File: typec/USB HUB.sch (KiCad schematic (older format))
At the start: 26 parts, among them U1 TPD6E05U06-USON, U2 TPD4E05U06-USON, U3 TPS62081-WSON, U4 TPD4E05U06-USON, U5 TPS74801-VSON, U6 TUSB212-X2QFN

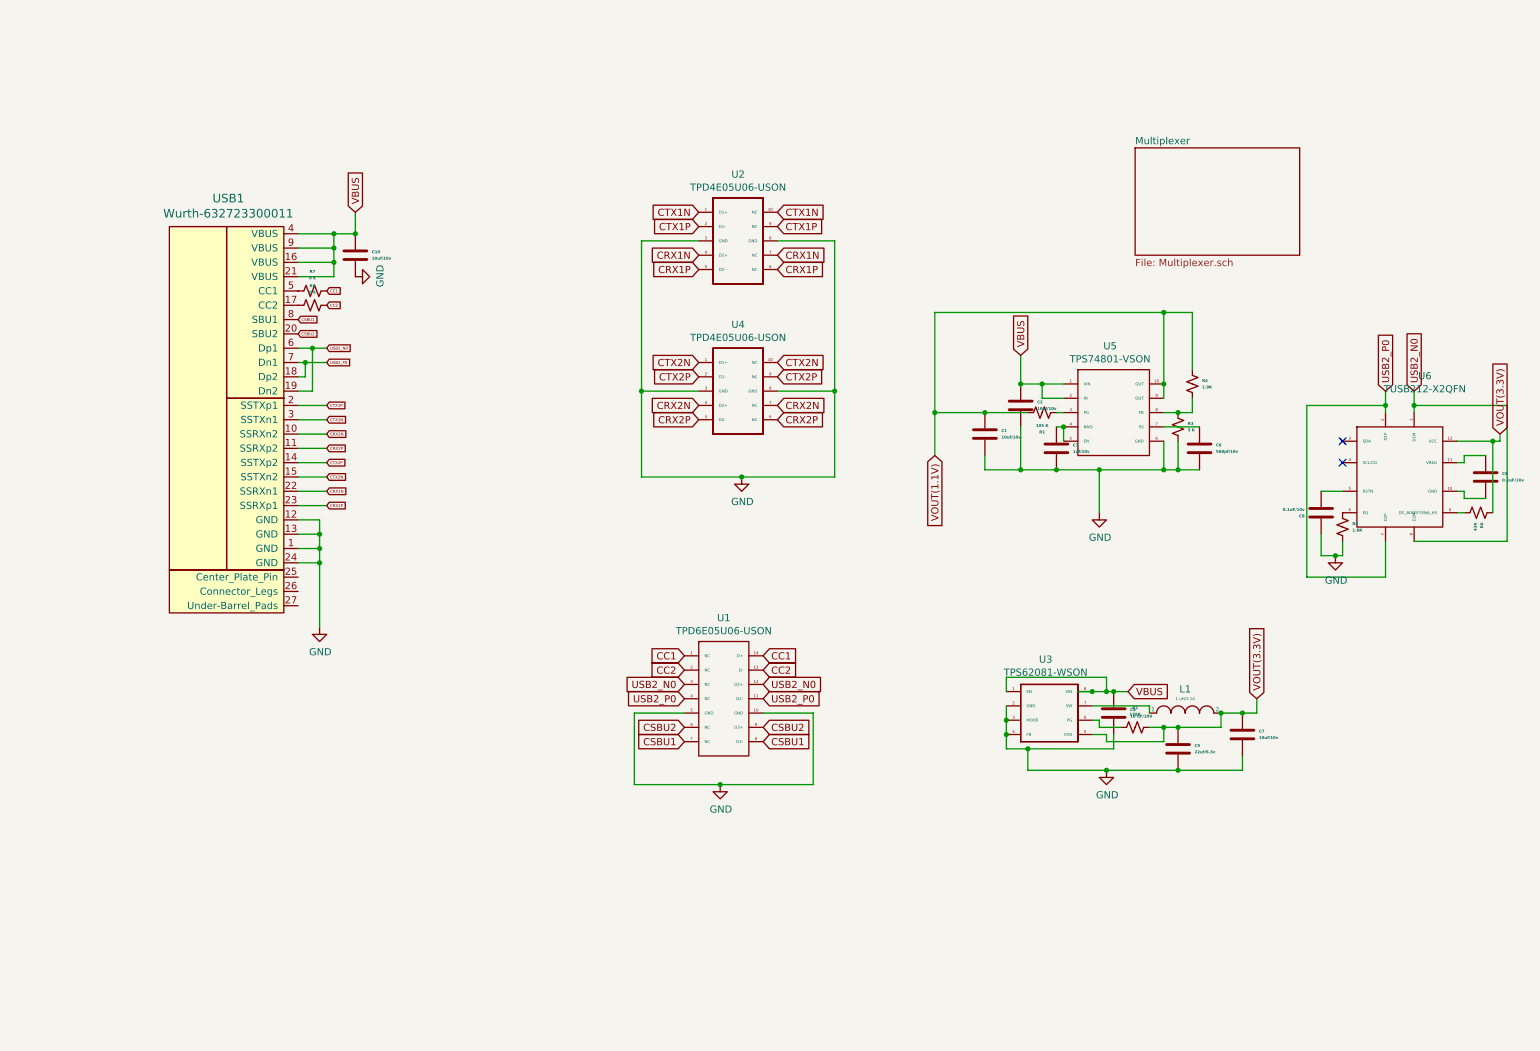
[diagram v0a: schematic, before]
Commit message: Added another page and completed the Multiplexer schematics.
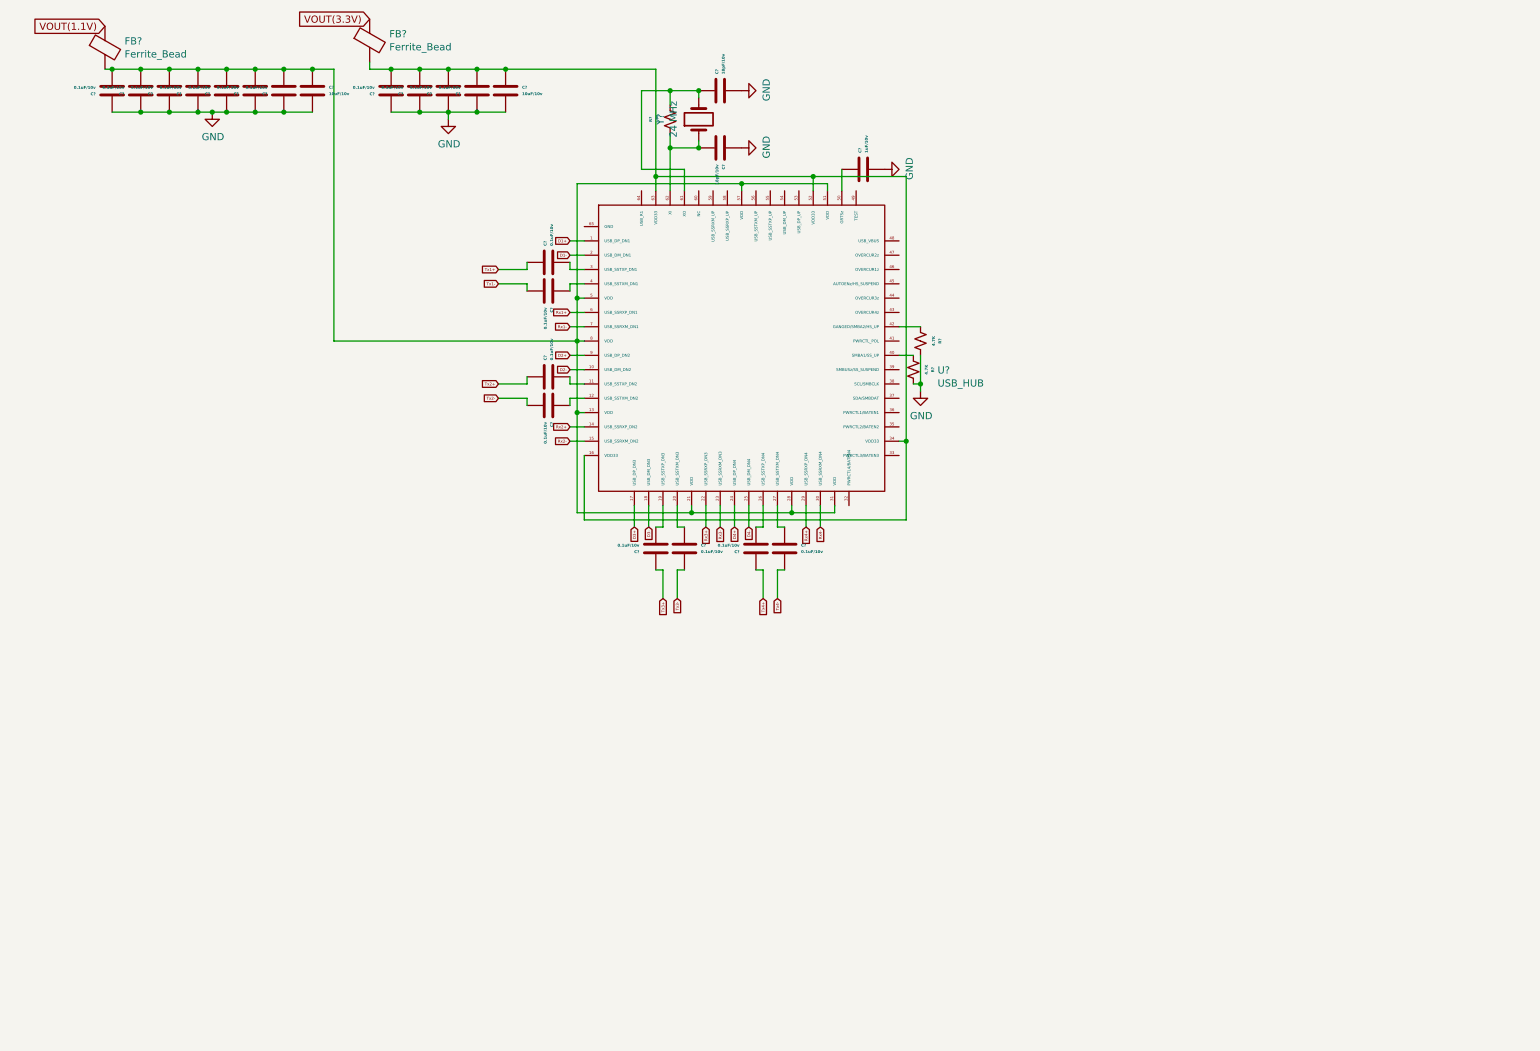
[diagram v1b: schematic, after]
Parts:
- removed C1, C10, C2, C7: 10uf/10v, Capacitor_SMD:C_0805_2012Metric, symbol Device:C
- removed C3: 1uf/10v, Capacitor_SMD:C_0402_1005Metric, symbol Device:C
- removed C4: 10 uF/10V, Capacitor_SMD:C_0805_2012Metric, symbol Device:C
- removed C5: 22uf/6.3v, Capacitor_SMD:C_0805_2012Metric, symbol Device:C
- removed C6: 560pf/10v, Capacitor_SMD:C_0402_1005Metric, symbol Device:C
- removed C8, C9: 0.1uF/10v, Capacitor_SMD:C_0402_1005Metric, symbol Device:C
- removed L1: 1 uH/3.1A, Inductor_SMD:L_6.3x6.3_H3, symbol pspice:INDUCTOR
- removed R1: 105 K, Resistor_SMD:R_0805_2012Metric, symbol Device:R_Small_US
- removed R2: 178K, Resistor_SMD:R_0805_2012Metric, symbol Device:R_Small_US
- removed R3: 5 K, Resistor_SMD:R_0805_2012Metric, symbol Device:R_Small_US
- removed R4: 1.9K, Resistor_SMD:R_0805_2012Metric, symbol Device:R_Small_US
- removed R5: 1.6K, Resistor_SMD:R_0805_2012Metric, symbol Device:R_Small_US
- removed R6: 43K, Resistor_SMD:R_0805_2012Metric, symbol Device:R_Small_US
- removed R7, R8: 0 E, Resistor_SMD:R_0805_2012Metric, symbol Device:R_Small_US
- removed U1: TPD6E05U06-USON, TPD6E05U06-USON:TPD6E05U06-USON, symbol TPD6E05U06-USON:TPD6E05U06-USON
- removed U2, U4: TPD4E05U06-USON, TPD4E05U06-USON:TPD4E05U06-USON, symbol TPD4E05U06-USON:TPD4E05U06-USON
- removed U3: TPS62081-WSON, TPS62081-WSON:TPS62081-WSON, symbol typec-rescue:TPS62081-WSON-TPS62081-WSON
- removed U5: TPS74801-VSON, TPS74801-VSON:TPS74801-VSON, symbol typec-rescue:TPS74801-VSON-TPS74801-VSON
- removed U6: TUSB212-X2QFN, TUSB212-X2QFN:TUSB212-X2QFN, symbol TUSB212-X2QFN:TUSB212-X2QFN
- removed USB1: Wurth-632723300011, Type-C:Wurth-632723300011-MaximumExtensionMount, symbol TYPEC_MODULES:Wurth-632723300011
- added C? (x11): 0.1uF/10v, Capacitor_SMD:C_1206_3216Metric, symbol Device:C
- added C? (x2): 10uF/10v, Capacitor_SMD:C_1206_3216Metric, symbol Device:C
- added C? (x8): 0.1uF/10v, Capacitor_SMD:C_0201_0603Metric, symbol Device:C
- added C? (x2): 18pF/10v, Capacitor_SMD:C_0603_1608Metric, symbol Device:C
- added C?: 1uF/10v, Capacitor_SMD:C_0805_2012Metric, symbol Device:C
- added FB? (x2): Ferrite_Bead, Inductor_SMD:L_0805_2012Metric, symbol Device:Ferrite_Bead
- added R? (x2): 4.7K, Resistor_SMD:R_0402_1005Metric, symbol Device:R_Small_US
- added R?: 1 M, Resistor_SMD:R_0805_2012Metric, symbol Device:R_Small_US
- added U?: USB_HUB, symbol TUSB8042-VQFN:USB_HUB
- added Y?: 24 MHz, Crystal:Crystal_SMD_3225-4Pin_3.2x2.5mm, symbol Device:Crystal
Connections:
- net GND: now also C?.1, C?.1, C?.1, C?.1, C?.1, C?.1, C?.1, C?.1, C?.1, C?.1, C?.1, C?.1, C?.2, C?.2, C?.2, C?.2, R?.1, R?.1
- net VOUT(1.1V): now also FB?.1
- net VOUT(3.3V): now also FB?.1
- new net: C?.2, U?.11 (USB_SSTXP_DN2)
- new net: C?.1, U?.12 (USB_SSTXM_DN2)
- new net: C?.1, C?.2, C?.2, C?.2, C?.2, C?.2, C?.2, C?.2, FB?.2, U?.13 (VDD), U?.21 (VDD), U?.28 (VDD), U?.31 (VDD), U?.5 (VDD), U?.51 (VDD), U?.57 (VDD), U?.8 (VDD)
- new net: C?.1, C?.2, C?.2, C?.2, C?.2, FB?.2, U?.16 (VDD33), U?.34 (VDD33), U?.52 (VDD33), U?.63 (VDD33)
- new net: C?.2, U?.19 (USB_SSTXP_DN3)
- new net: C?.1, U?.20 (USB_SSTXM_DN3)
- new net: C?.2, U?.26 (USB_SSTXP_DN4)
- new net: C?.1, U?.27 (USB_SSTXM_DN4)
- new net: C?.2, U?.3 (USB_SSTXP_DN1)
- new net: C?.1, U?.4 (USB_SSTXM_DN1)
- new net: R?.2, U?.40 (SMBA1/SS_UP)
- new net: R?.2, U?.42 (GANGED/SMBA2/HS_UP)
- new net: C?.1, U?.50 (GRTSz)
- new net: C?.1, R?.1, U?.61 (XO), Y?.2
- new net: C?.2, R?.2, U?.62 (XI), Y?.1
- new net D1+: U?.1 (USB_DP_DN1)
- new net D1-: U?.2 (USB_DM_DN1)
- new net D2+: U?.9 (USB_DP_DN2)
- new net D2-: U?.10 (USB_DM_DN2)
- new net D3+: U?.17 (USB_DP_DN3)
- new net D3-: U?.18 (USB_DM_DN3)
- new net D4+: U?.24 (USB_DP_DN4)
- new net D4-: U?.25 (USB_DM_DN4)
- new net Rx1+: U?.6 (USB_SSRXP_DN1)
- new net Rx1-: U?.7 (USB_SSRXM_DN1)
- new net Rx2+: U?.14 (USB_SSRXP_DN2)
- new net Rx2-: U?.15 (USB_SSRXM_DN2)
- new net Rx3+: U?.22 (USB_SSRXP_DN3)
- new net Rx3-: U?.23 (USB_SSRXM_DN3)
- new net Rx4+: U?.29 (USB_SSRXP_DN4)
- new net Rx4-: U?.30 (USB_SSRXM_DN4)
- new net Tx1+: C?.1
- new net Tx1-: C?.2
- new net Tx2+: C?.1
- new net Tx2-: C?.2
- new net Tx3+: C?.1
- new net Tx3-: C?.2
- new net Tx4+: C?.1
- new net Tx4-: C?.2
- no-connect marks 2 -> 0

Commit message: Last minute changes
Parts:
- U7: renamed from U?; footprint (none) -> TUSB8042-VQFN:QFN-64-1EP_9x9mm_P0.5mm_EP6x6mm_ThermalVias
- gave numbers to parts that had none: 30

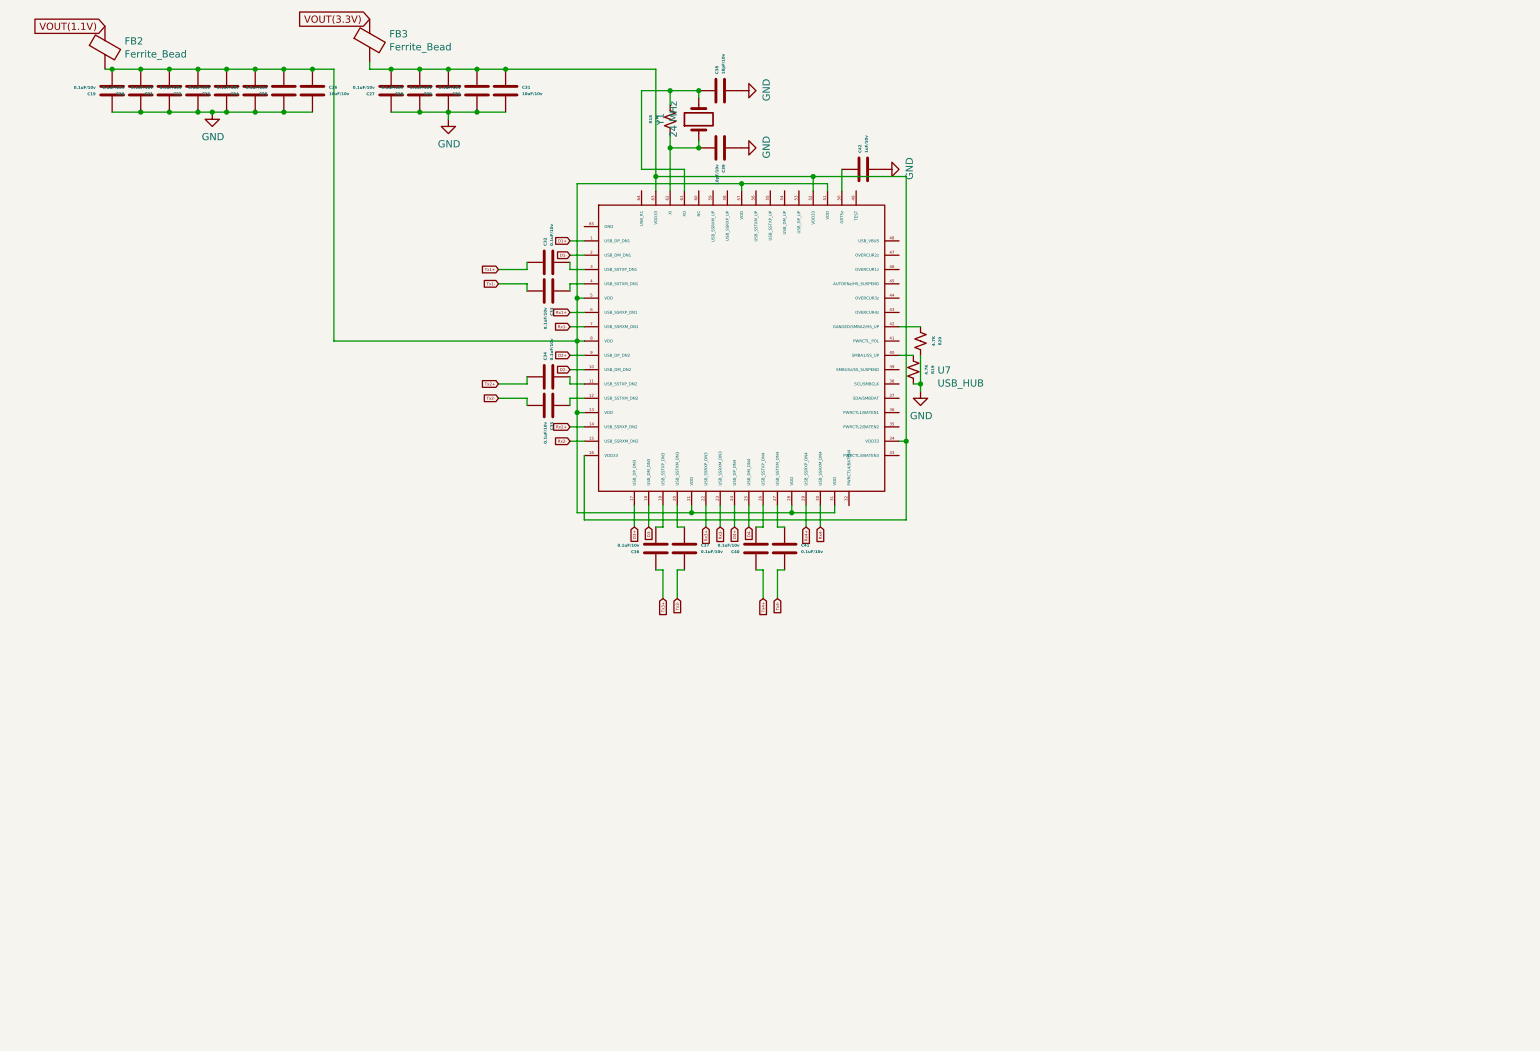
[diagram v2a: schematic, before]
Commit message: USB HUB IC ADDED
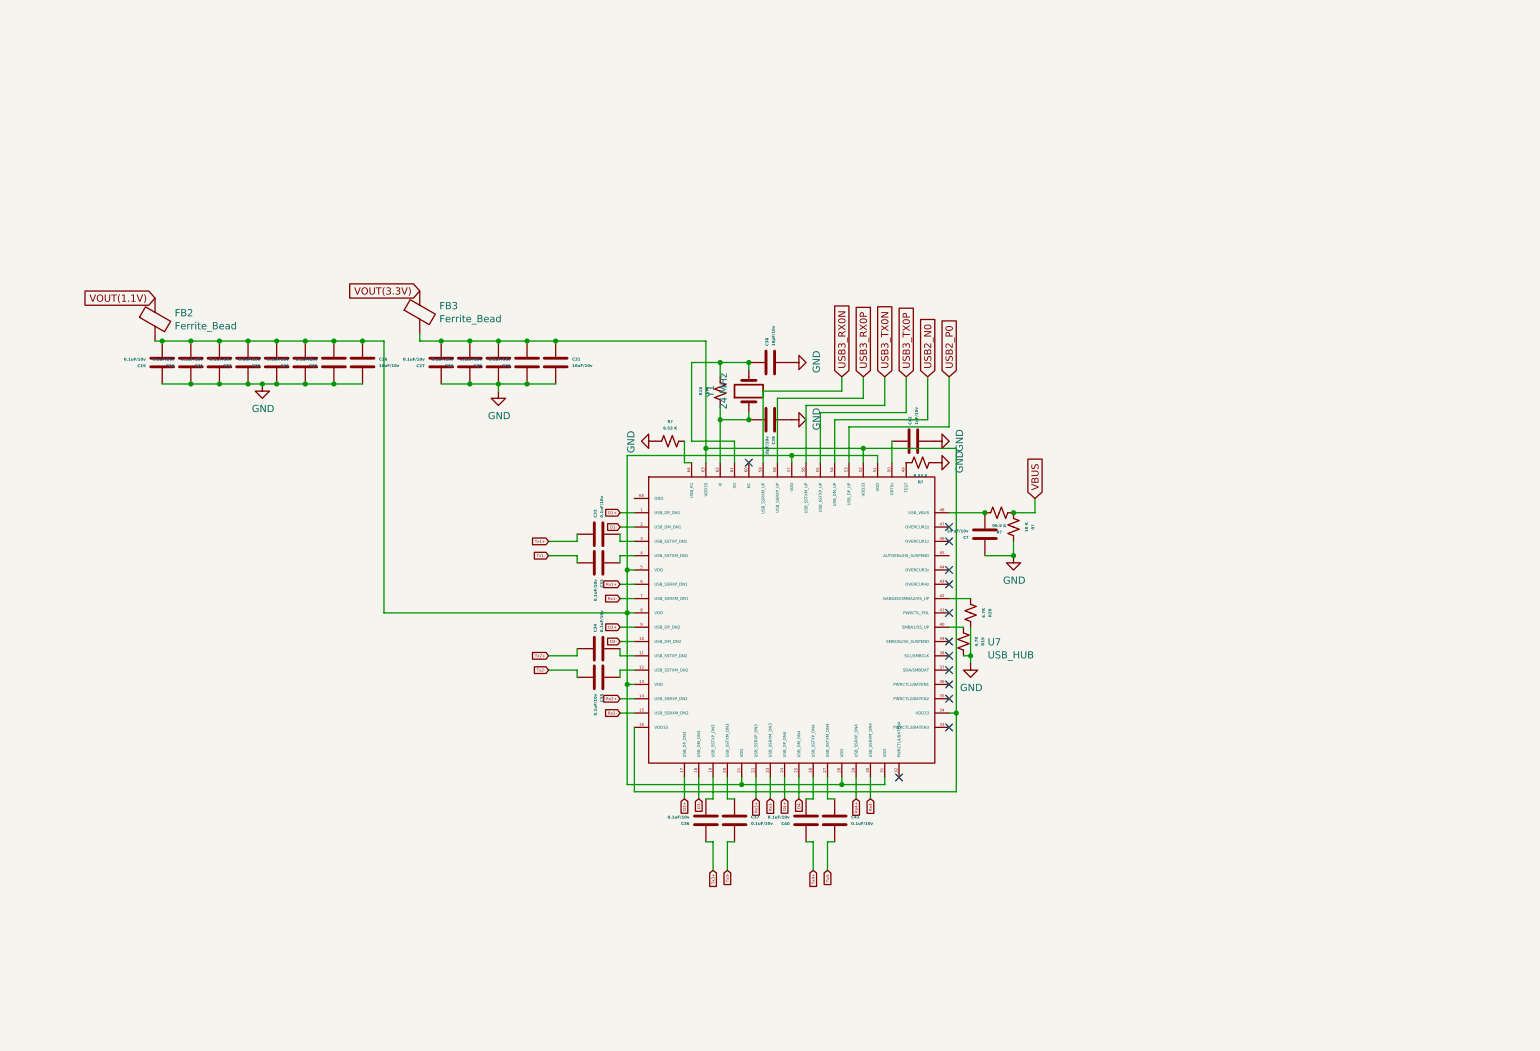
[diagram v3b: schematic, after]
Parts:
- added C?: 10 uF/10v, Capacitor_SMD:C_0805_2012Metric, symbol Device:C
- added R?: 90.9 K, Resistor_SMD:R_0805_2012Metric, symbol Device:R_Small_US
- added R?: 10 K, Resistor_SMD:R_0402_1005Metric, symbol Device:R_Small_US
- added R? (x2): 9.53 K, Resistor_SMD:R_0402_1005Metric, symbol Device:R_Small_US
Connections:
- net GND: now also C?.1, R?.1, R?.2, R?.2
- net at U7.48 (USB_VBUS): now also C?.2, R?.1
- net at U7.49 (TEST): now also R?.1
- net USB2_P0: now reaches U7.53 (USB_DP_UP)
- net USB2_N0: now reaches U7.54 (USB_DM_UP)
- net USB3_TX0P: now reaches U7.55 (USB_SSTXP_UP)
- net USB3_TX0N: now reaches U7.56 (USB_SSTXM_UP)
- net USB3_RX0P: now reaches U7.58 (USB_SSRXP_UP)
- net USB3_RX0N: now reaches U7.59 (USB_SSRXM_UP)
- net at U7.64 (USB_R1): now also R?.1
- new net VBUS: R?.2, R?.2
- no-connect marks 0 -> 13
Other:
- moved on the sheet: C19, C20, C21, C22, C23, C24, C25, C26, C27, C28, C29, C30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
